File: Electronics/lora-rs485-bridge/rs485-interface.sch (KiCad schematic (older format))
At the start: 4 parts, among them U1 SN65HVD72

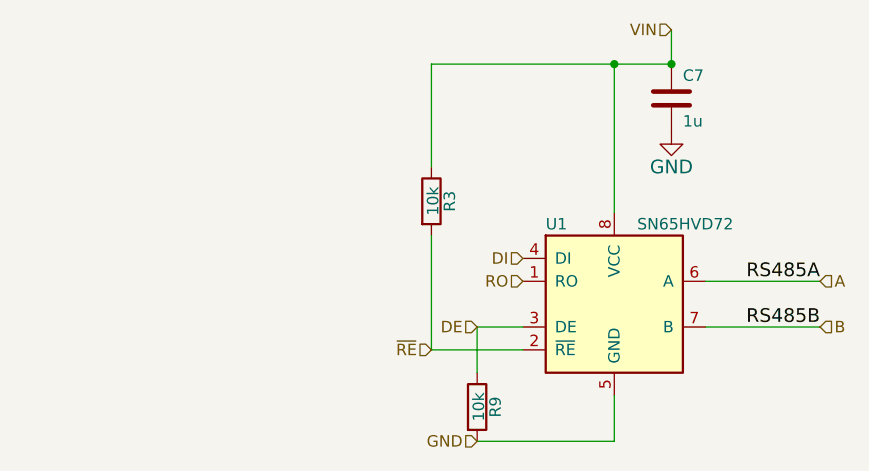
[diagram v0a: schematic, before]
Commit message: Some PCB routing is done
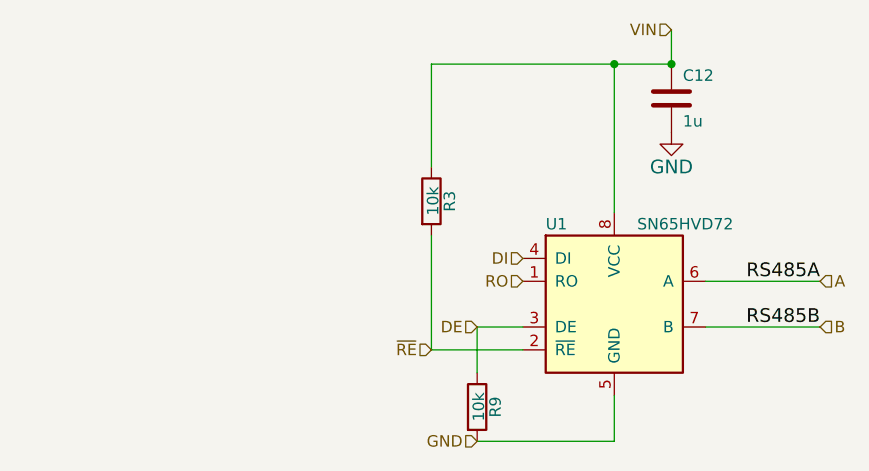
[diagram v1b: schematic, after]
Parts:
- C12: renamed from C7; footprint Capacitors_SMD:C_0603 -> Capacitor_SMD:C_0603_1608Metric; Comment (none) -> Generic X5R capacitor
- R3, R9: footprint Resistors_SMD:R_0603 -> Resistor_SMD:R_0603_1608Metric; Comment (none) -> Generic 5% resistor
- U1: footprint Housings_SOIC:SOIC-8_3.9x4.9mm_Pitch1.27mm -> Package_SO:SOIC-8_3.9x4.9mm_P1.27mm
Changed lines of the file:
@@
 EESchema Schematic File Version 5
-LIBS:lora-bridge-cache
 EELAYER 30 0
 EELAYER END
 $Descr A4 11693 8268
 encoding utf-8
-Sheet 3 5
+Sheet 2 5
 Title ""
 Date ""
@@
 ~RE
 $Comp
-L Device:C C7
+L Device:C C12
 U 1 1 54DF0C76
 P 4025 1400
-F 0 "C7" H 4075 1500 50  0000 L CNN
+F 0 "C12" H 4075 1500 50  0000 L CNN
 F 1 "1u" H 4075 1300 50  0000 L CNN
-F 2 "Capacitors_SMD:C_0603" H 4063 1250 30  0001 C CNN
+F 2 "Capacitor_SMD:C_0603_1608Metric" H 4063 1250 30  0001 C CNN
 F 3 "" H 4025 1400 60  0000 C CNN
+F 4 "Generic X5R capacitor" H 4025 1400 50  0001 C CNN "Comment"
 	1    4025 1400
 	1    0    0    -1
 $EndComp
 $Comp
-L power:GND #PWR18
+L power:GND #PWR018
 U 1 1 54DF0CCD
 P 4025 1550
-F 0 "#PWR18" H 4025 1300 60  0001 C CNN
+F 0 "#PWR018" H 4025 1300 60  0001 C CNN
 F 1 "GND" H 4025 1400 60  0000 C CNN
 F 2 "" H 4025 1550 60  0000 C CNN
@@
 F 0 "R9" V 3255 2750 50  0000 C CNN
 F 1 "10k" V 3182 2751 50  0000 C CNN
-F 2 "Resistors_SMD:R_0603" V 3105 2750 30  0001 C CNN
+F 2 "Resistor_SMD:R_0603_1608Metric" V 3105 2750 30  0001 C CNN
 F 3 "" H 3175 2750 30  0000 C CNN
+F 4 "Generic 5% resistor" H 3175 2750 50  0001 C CNN "Comment"
 	1    3175 2750
 	1    0    0    -1
@@
 F 0 "R3" V 3055 1850 50  0000 C CNN
 F 1 "10k" V 2982 1851 50  0000 C CNN
-F 2 "Resistors_SMD:R_0603" V 2905 1850 30  0001 C CNN
+F 2 "Resistor_SMD:R_0603_1608Metric" V 2905 1850 30  0001 C CNN
 F 3 "" H 2975 1850 30  0000 C CNN
+F 4 "Generic 5% resistor" H 2975 1850 50  0001 C CNN "Comment"
 	1    2975 1850
 	1    0    0    -1
@@
 F 0 "U1" H 3475 2650 50  0000 L CNN
 F 1 "SN65HVD72" H 3875 2650 50  0000 L CNN
-F 2 "Housings_SOIC:SOIC-8_3.9x4.9mm_Pitch1.27mm" H 3775 2300 50  0001 C CIN
+F 2 "Package_SO:SOIC-8_3.9x4.9mm_P1.27mm" H 3775 2300 50  0001 C CIN
 F 3 "" H 3775 2300 60  0000 C CNN
 F 4 "SN65HVD72DR" H 3775 2300 60  0001 C CNN "PartNo"

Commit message: Add ESD protection to i2c lines, change VIN TVS diode to higher voltage, add series resistors to SPI lines, compress the PCB to be at width of typical 4xAA battery holder
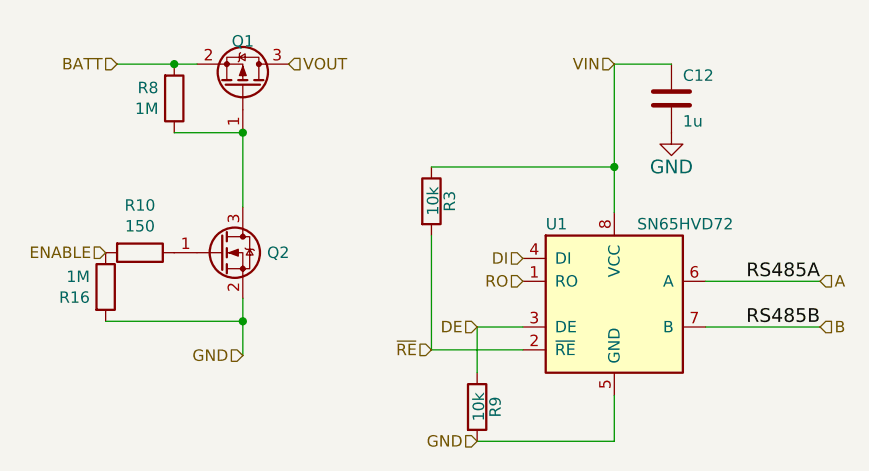
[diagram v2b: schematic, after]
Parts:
- added Q1: Q_PMOS_GSD, Package_TO_SOT_SMD:SOT-23, symbol Device:Q_PMOS_GSD
- added Q2: Q_NMOS_GSD, Package_TO_SOT_SMD:SOT-23, symbol Device:Q_NMOS_GSD
- added R10: 150, Resistor_SMD:R_0603_1608Metric, symbol Device:R
- added R16, R8: 1M, Resistor_SMD:R_0603_1608Metric, symbol Device:R
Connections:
- net GND: now also Q2.2 (S), R16.2
- new net: Q2.1 (G), R10.1
- new net: Q1.1 (G), Q2.3 (D), R8.1
- new net BATT: Q1.2 (S), R8.2
- new net ENABLE: R10.2, R16.1
- new net VOUT: Q1.3 (D)
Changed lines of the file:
@@
 $Descr A4 11693 8268
 encoding utf-8
-Sheet 2 5
+Sheet 5 5
 Title ""
 Date ""
@@
 Text HLabel 4675 2400 2    50   Input ~ 0
 B
-Text HLabel 4025 1100 0    50   Input ~ 0
-VIN
 Text HLabel 3175 2900 0    50   Input ~ 0
 GND
@@
 RS485B
 Wire Wire Line
-	3775 1900 3775 1250
-Wire Wire Line
-	2975 1250 3775 1250
+	3775 1900 3775 1700
 Wire Wire Line
 	4175 2200 4675 2200
 Wire Wire Line
 	4175 2400 4675 2400
-Connection ~ 3775 1250
 $Comp
 L Device:R R9
@@
 	1    0    0    -1
 $EndComp
-Wire Wire Line
-	2975 1250 2975 1700
 Wire Wire Line
 	2975 2000 2975 2500
@@
 	1    0    0    -1
 $EndComp
-Wire Wire Line
-	4025 1100 4025 1250
-Connection ~ 4025 1250
+Text HLabel 3775 1250 0    50   Input ~ 0
+VIN
+Text HLabel 1550 2075 0    50   Input ~ 0
+ENABLE
+$Comp
+L Device:R R8
+U 1 1 5D8C5F68
+P 1850 1400
+F 0 "R8" H 1781 1354 50  0000 R CNN
+F 1 "1M" H 1781 1445 50  0000 R CNN
+F 2 "Resistor_SMD:R_0603_1608Metric" V 1780 1400 50  0001 C CNN
+F 3 "~" H 1850 1400 50  0001 C CNN
+	1    1850 1400
+	1    0    0    1
+$EndComp
+Wire Wire Line
+	1850 1250 1950 1250
+Wire Wire Line
+	2150 1875 2150 1550
+Wire Wire Line
+	1600 1250 1850 1250
+Connection ~ 1850 1250
+$Comp
+L Device:Q_PMOS_GSD Q1
+U 1 1 5D8C5F67
+P 2150 1350
+F 0 "Q1" V 2350 1350 50  0000 C CNN
+F 1 "Q_PMOS_GSD" V 2387 1350 50  0001 C CNN
+F 2 "Package_TO_SOT_SMD:SOT-23" H 2350 1450 29  0001 C CNN
+F 3 "" H 2150 1350 60  0000 C CNN
+F 4 "NX2301P,215 " H 2150 1350 60  0001 C CNN "PartNo"
+F 5 "NXP" H 2150 1350 60  0001 C CNN "Manufacturer"
+F 6 "1894738" H 2150 1350 60  0001 C CNN "Distributor"
+F 7 "Exact as specified" H 2150 1350 50  0001 C CNN "Comment"
+	1    2150 1350
+	0    1    -1   0
+$EndComp
+Text HLabel 2350 1250 2    50   Input ~ 0
+VOUT
+Text HLabel 1600 1250 0    50   Input ~ 0
+BATT
+Wire Wire Line
+	2975 1700 3775 1700
+Connection ~ 3775 1700
+Wire Wire Line
+	3775 1700 3775 1250
+$Comp
+L Device:R R10
+U 1 1 5DC0D0CD
+P 1700 2075
+F 0 "R10" V 1493 2075 50  0000 C CNN
+F 1 "150" V 1584 2075 50  0000 C CNN
+F 2 "Resistor_SMD:R_0603_1608Metric" V 1630 2075 50  0001 C CNN
+F 3 "~" H 1700 2075 50  0001 C CNN
+	1    1700 2075
+	0    1    1    0
+$EndComp
+$Comp
+L Device:Q_NMOS_GSD Q2
+U 1 1 5C9CE926
+P 2050 2075
+F 0 "Q2" H 2256 2075 50  0000 L CNN
+F 1 "Q_NMOS_GSD" H 2256 2030 50  0001 L CNN
+F 2 "Package_TO_SOT_SMD:SOT-23" H 2250 2175 50  0001 C CNN
+F 3 "~" H 2050 2075 50  0001 C CNN
+F 4 "NTR4003NT1G" H 2050 2075 50  0001 C CNN "PartNo"
+F 5 "ON SEMICONDUCTOR" H 2050 2075 50  0001 C CNN "Manufacturer"
+	1    2050 2075
+	1    0    0    -1
+$EndComp
+Wire Wire Line
+	1850 1550 2150 1550
+Connection ~ 2150 1550
+$Comp
+L Device:R R16
+U 1 1 5D8F7219
+P 1550 2225
+F 0 "R16" H 1481 2179 50  0000 R CNN
+F 1 "1M" H 1481 2270 50  0000 R CNN
+F 2 "Resistor_SMD:R_0603_1608Metric" V 1480 2225 50  0001 C CNN
+F 3 "~" H 1550 2225 50  0001 C CNN
+	1    1550 2225
+	1    0    0    -1
+$EndComp
+Text HLabel 2150 2525 0    50   Input ~ 0
+GND
+Wire Wire Line
+	2150 2275 2150 2375
+Connection ~ 2150 2375
+Wire Wire Line
+	2150 2375 2150 2525
+Wire Wire Line
+	1550 2375 2150 2375
 $EndSCHEMATC

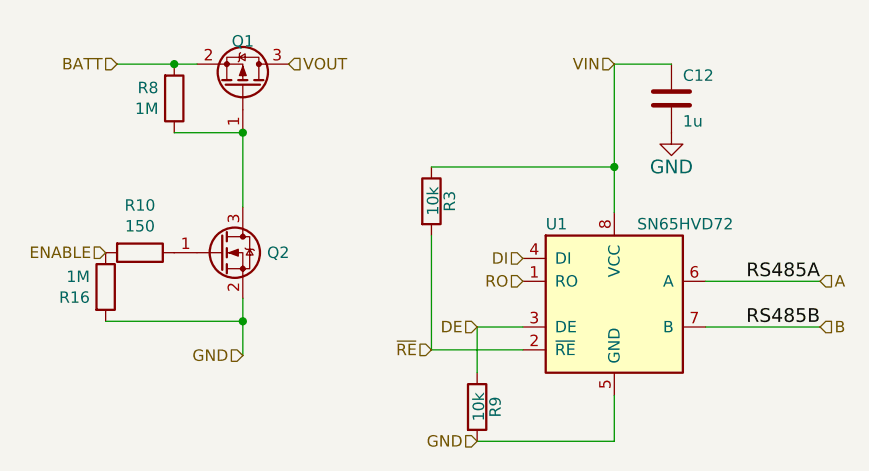
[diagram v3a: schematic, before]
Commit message: Update D3 to silicone diode as schottky leaks as hell; Add D2 to protect gates of mosfets; Remove series resistors from RFM95 interface, add pullups/downs for better sleep stability; Unify resistor values across the board; Bump version number to v1.2
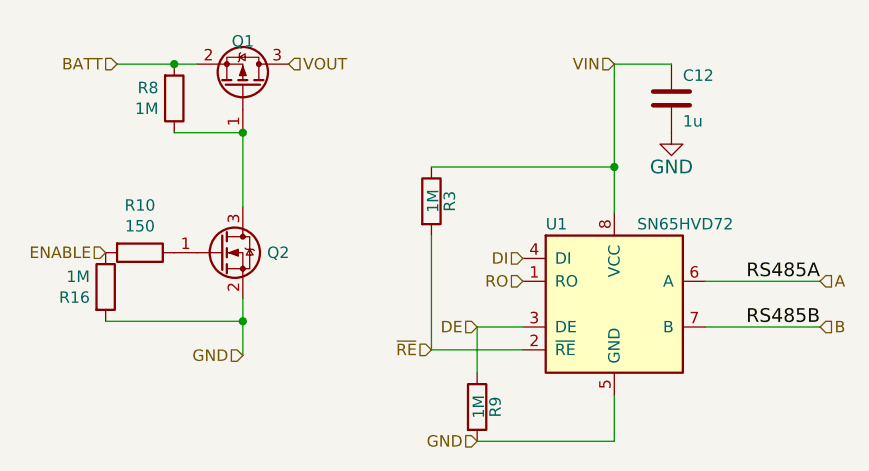
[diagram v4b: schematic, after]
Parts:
- R3, R9: value 10k -> 1M
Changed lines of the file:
@@
 $Descr A4 11693 8268
 encoding utf-8
-Sheet 5 5
+Sheet 4 5
 Title ""
 Date ""
@@
 P 3175 2750
 F 0 "R9" V 3255 2750 50  0000 C CNN
-F 1 "10k" V 3182 2751 50  0000 C CNN
+F 1 "1M" V 3182 2751 50  0000 C CNN
 F 2 "Resistor_SMD:R_0603_1608Metric" V 3105 2750 30  0001 C CNN
 F 3 "" H 3175 2750 30  0000 C CNN
@@
 P 2975 1850
 F 0 "R3" V 3055 1850 50  0000 C CNN
-F 1 "10k" V 2982 1851 50  0000 C CNN
+F 1 "1M" V 2982 1851 50  0000 C CNN
 F 2 "Resistor_SMD:R_0603_1608Metric" V 2905 1850 30  0001 C CNN
 F 3 "" H 2975 1850 30  0000 C CNN
@@
 	2975 1700 3775 1700
 Wire Wire Line
-	2150 1875 2150 1550
-Wire Wire Line
 	1600 1250 1850 1250
 Text HLabel 1600 1250 0    50   Input ~ 0
 BATT
+Wire Wire Line
+	1850 1250 1950 1250
+Connection ~ 1850 1250
+Wire Wire Line
+	2150 1875 2150 1550
 Wire Wire Line
 	1850 1550 2150 1550
@@
 	1    0    0    1
 $EndComp
-Wire Wire Line
-	1850 1250 1950 1250
-Connection ~ 1850 1250
 $Comp
 L Device:Q_PMOS_GSD Q1
